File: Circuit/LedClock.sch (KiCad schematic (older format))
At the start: 24 parts, among them K1 PROG, SW1 MSP_RESET, U1 MSP430G2553IPW20

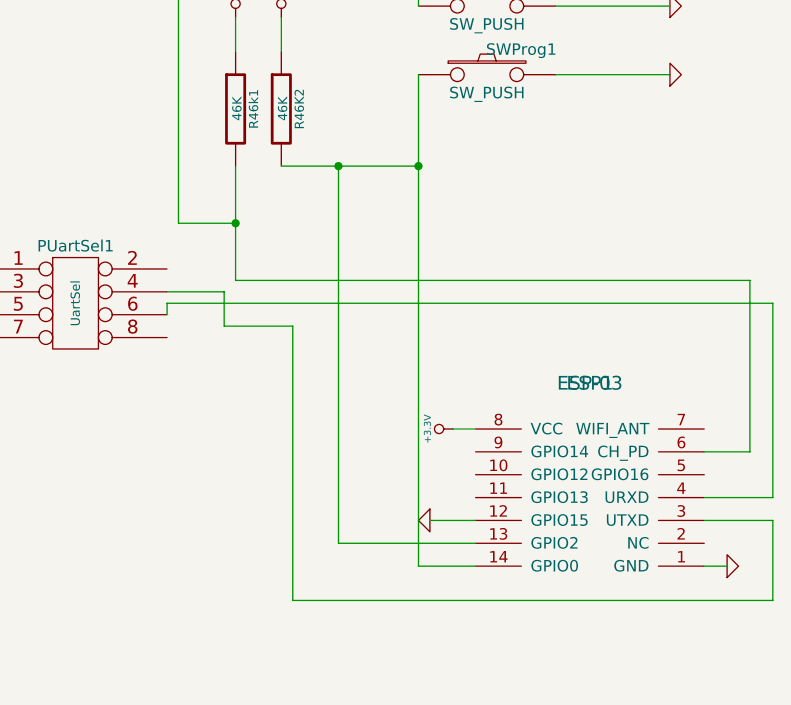
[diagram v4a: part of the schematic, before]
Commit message: Updated pcb layout and circuit, found 1 flaw in the design
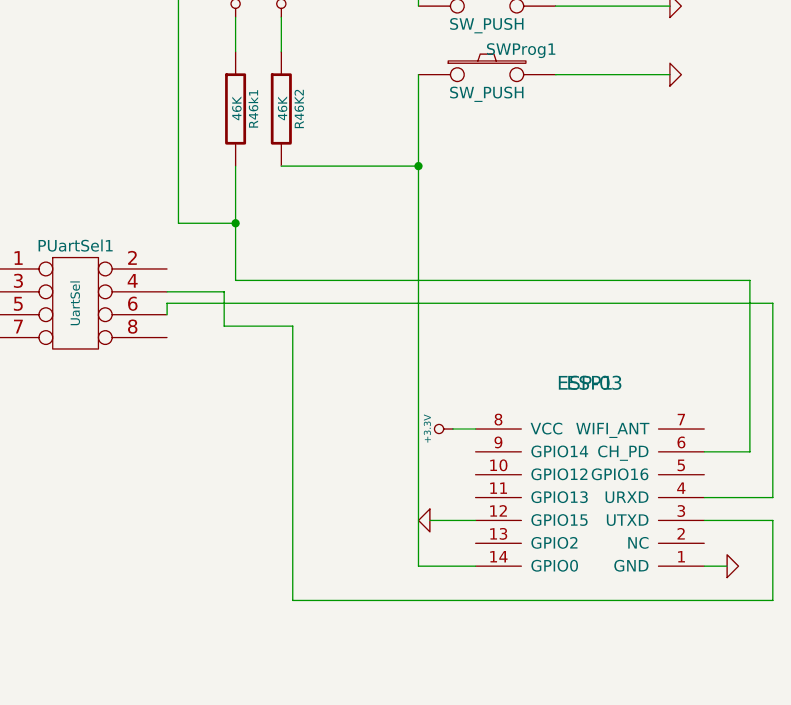
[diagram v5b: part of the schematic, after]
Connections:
- net at ESP1.14 (GPIO0), R46K2.2, SWProg1.1: no longer ESP1.13 (GPIO2)
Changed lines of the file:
@@
 Sheet 1 1
 Title ""
-Date "10 jan 2016"
+Date "20 feb 2016"
 Rev ""
 Comp ""
@@
 	9150 3300 9150 3500
 Connection ~ 8350 4450
-Connection ~ 8800 4200
 Wire Wire Line
 	5000 950  5000 900
@@
 	8300 4900 8600 4900
 Wire Wire Line
-	8800 5850 9400 5850
-Wire Wire Line
 	8350 4700 10600 4700
 Wire Wire Line
@@
 	10600 5450 10400 5450
 Wire Wire Line
-	8800 4200 8800 5850
-Wire Wire Line
 	9150 5950 9400 5950
